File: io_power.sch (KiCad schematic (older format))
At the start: 15 parts

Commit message: Done adding the kitchen sink
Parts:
- added U?: TCA6424A, symbol antboard:TCA6424A
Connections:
- net GND: now also U?.25 (GND), U?.26 (ADDR)
- net PAV10: now also U?.3 (P02)
- net PAV160: now also U?.7 (P06)
- net PAV20: now also U?.4 (P03)
- net PAV40: now also U?.5 (P04)
- net PAV5: now also U?.2 (P01)
- net PAV80: now also U?.6 (P05)
- net PAVEN: now also U?.1 (P00)
- net PBV10: now also U?.10 (P11), U?.17 (P20)
- net PBV160: now also U?.14 (P15), U?.21 (P24)
- net PBV20: now also U?.11 (P12), U?.18 (P21)
- net PBV40: now also U?.12 (P13), U?.19 (P22)
- net PBV5: now also U?.16 (P17), U?.9 (P10)
- net PBV80: now also U?.13 (P14), U?.20 (P23)
- net PBVEN: now also U?.15 (P16), U?.8 (P07)
- net SCL: now also U?.29 (SCL)
- net SDA: now also U?.30 (SDA)
- new net +3V3: U?.27 (VCCP), U?.28 (~RST), U?.31 (VCCI)
- no-connect marks 3 -> 4
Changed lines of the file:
@@
 EESchema Schematic File Version 4
-LIBS:antboard-cache
 EELAYER 30 0
 EELAYER END
@@
 encoding utf-8
 Sheet 5 5
-Title ""
-Date ""
+Title "I/O power supplies"
+Date "2019-11-29"
 Rev ""
 Comp ""
@@
 SCL
 Wire Wire Line
-	1100 1200 1600 1200
-Text Label 1600 1200 2    50   ~ 0
-PAVEN
-Text HLabel 1100 1200 0    50   Input ~ 0
-PAVEN
-Wire Wire Line
-	1100 1300 1600 1300
-Text Label 1600 1300 2    50   ~ 0
-PBVEN
-Text HLabel 1100 1300 0    50   Input ~ 0
-PBVEN
-Wire Wire Line
-	1100 1400 1600 1400
-Text Label 1600 1400 2    50   ~ 0
-PCVEN
-Text HLabel 1100 1400 0    50   Input ~ 0
-PCVEN
-Wire Wire Line
 	7350 5800 7350 5900
 $Comp
@@
 Text Label 6550 5500 0    50   ~ 0
 PBV160
-Wire Wire Line
-	7550 5500 6550 5500
 Text Label 6550 5400 0    50   ~ 0
 PBV80
-Wire Wire Line
-	7550 5400 6550 5400
 Text Label 6550 5300 0    50   ~ 0
 PBV40
-Wire Wire Line
-	7550 5300 6550 5300
 Text Label 6550 5200 0    50   ~ 0
 PBV20
-Wire Wire Line
-	7550 5200 6550 5200
 Text Label 6550 5100 0    50   ~ 0
 PBV10
-Wire Wire Line
-	7550 5100 6550 5100
 Text Label 6550 5000 0    50   ~ 0
 PBV5
-Wire Wire Line
-	7550 5000 6550 5000
 Text Label 6550 3050 0    50   ~ 0
 PBVEN
@@
 Text Label 6550 3750 0    50   ~ 0
 PBV160
-Wire Wire Line
-	7550 3750 6550 3750
 Text Label 6550 3650 0    50   ~ 0
 PBV80
-Wire Wire Line
-	7550 3650 6550 3650
 Text Label 6550 3550 0    50   ~ 0
 PBV40
-Wire Wire Line
-	7550 3550 6550 3550
 Text Label 6550 3450 0    50   ~ 0
 PBV20
-Wire Wire Line
-	7550 3450 6550 3450
 Text Label 6550 3350 0    50   ~ 0
 PBV10
-Wire Wire Line
-	7550 3350 6550 3350
 Text Label 6550 3250 0    50   ~ 0
 PBV5
-Wire Wire Line
-	7550 3250 6550 3250
 Text Label 6550 1300 0    50   ~ 0
 PAVEN
@@
 Text Label 6550 2000 0    50   ~ 0
 PAV160
-Wire Wire Line
-	7550 2000 6550 2000
 Text Label 6550 1900 0    50   ~ 0
 PAV80
-Wire Wire Line
-	7550 1900 6550 1900
 Text Label 6550 1800 0    50   ~ 0
 PAV40
-Wire Wire Line
-	7550 1800 6550 1800
 Text Label 6550 1700 0    50   ~ 0
 PAV20
-Wire Wire Line
-	7550 1700 6550 1700
 Text Label 6550 1600 0    50   ~ 0
 PAV10
-Wire Wire Line
-	7550 1600 6550 1600
 Text Label 6550 1500 0    50   ~ 0
 PAV5
-Wire Wire Line
-	7550 1500 6550 1500
 $Comp
 L Device:R_Small R?
@@
 Connection ~ 7000 4800
 Wire Wire Line
-	7000 4800 6550 4800
-Wire Wire Line
 	7000 3850 7000 3050
 Connection ~ 7000 3050
 Wire Wire Line
-	7000 3050 6550 3050
-Wire Wire Line
 	7000 2100 7000 1300
 Connection ~ 7000 1300
-Wire Wire Line
-	7000 1300 6550 1300
 Wire Wire Line
 	7000 2300 7000 2400
@@
 	1    0    0    -1
 $EndComp
+Wire Wire Line
+	4500 2550 5150 2550
+Wire Wire Line
+	4500 2650 5250 2650
+Wire Wire Line
+	5250 2650 5250 1600
+Wire Wire Line
+	5250 1600 7550 1600
+Wire Wire Line
+	4500 2750 5350 2750
+Wire Wire Line
+	5350 2750 5350 1700
+Wire Wire Line
+	5350 1700 7550 1700
+Wire Wire Line
+	4500 2850 5450 2850
+Wire Wire Line
+	5450 2850 5450 1800
+Wire Wire Line
+	5450 1800 7550 1800
+Wire Wire Line
+	5550 1900 5550 2950
+Wire Wire Line
+	5550 2950 4500 2950
+Wire Wire Line
+	5550 1900 7550 1900
+Wire Wire Line
+	4500 3050 5650 3050
+Wire Wire Line
+	5650 3050 5650 2000
+Wire Wire Line
+	5650 2000 7550 2000
+Wire Wire Line
+	4500 3250 7550 3250
+Wire Wire Line
+	4500 3350 7550 3350
+Wire Wire Line
+	4500 3450 7550 3450
+Wire Wire Line
+	4500 3550 7550 3550
+Wire Wire Line
+	4500 3650 7550 3650
+Wire Wire Line
+	4500 3750 7550 3750
+Wire Wire Line
+	5150 1500 7550 1500
+Wire Wire Line
+	5150 2550 5150 1500
+Wire Wire Line
+	4500 3950 5650 3950
+Wire Wire Line
+	5650 3950 5650 5000
+Wire Wire Line
+	5650 5000 7550 5000
+Wire Wire Line
+	5550 5100 5550 4050
+Wire Wire Line
+	5550 4050 4500 4050
+Wire Wire Line
+	5550 5100 7550 5100
+Wire Wire Line
+	4500 4150 5450 4150
+Wire Wire Line
+	5450 4150 5450 5200
+Wire Wire Line
+	5450 5200 7550 5200
+Wire Wire Line
+	5350 5300 5350 4250
+Wire Wire Line
+	5350 4250 4500 4250
+Wire Wire Line
+	5350 5300 7550 5300
+Wire Wire Line
+	4500 4350 5250 4350
+Wire Wire Line
+	5250 4350 5250 5400
+Wire Wire Line
+	5250 5400 7550 5400
+Wire Wire Line
+	5150 5500 5150 4450
+Wire Wire Line
+	5150 4450 4500 4450
+Wire Wire Line
+	5150 5500 7550 5500
+Wire Wire Line
+	3550 3350 3050 3350
+Wire Wire Line
+	3550 3450 3050 3450
+Text Label 3050 3350 0    50   ~ 0
+SDA
+Text Label 3050 3450 0    50   ~ 0
+SCL
+NoConn ~ 3550 3150
+$Comp
+L power:+3V3 #PWR?
+U 1 1 5DE774F4
+P 4050 2150
+F 0 "#PWR?" H 4050 2000 50  0001 C CNN
+F 1 "+3V3" H 4065 2323 50  0000 C CNN
+F 2 "" H 4050 2150 50  0001 C CNN
+F 3 "" H 4050 2150 50  0001 C CNN
+	1    4050 2150
+	1    0    0    -1
+$EndComp
+Wire Wire Line
+	4000 2250 4000 2200
+Wire Wire Line
+	4000 2200 4050 2200
+Wire Wire Line
+	4100 2200 4100 2250
+Wire Wire Line
+	4050 2150 4050 2200
+Connection ~ 4050 2200
+Wire Wire Line
+	4050 2200 4100 2200
+$Comp
+L power:GND #PWR?
+U 1 1 5DE8B0E0
+P 4050 4950
+AR Path="/5DE8B0E0" Ref="#PWR?"  Part="1"
+AR Path="/5DF7E971/5DE8B0E0" Ref="#PWR?"  Part="1"
+AR Path="/5DFC2583/5DE8B0E0" Ref="#PWR?"  Part="1"
+AR Path="/5EA8F1AB/5DE8B0E0" Ref="#PWR?"  Part="1"
+F 0 "#PWR?" H 4050 4700 50  0001 C CNN
+F 1 "GND" H 4055 4777 50  0000 C CNN
+F 2 "" H 4050 4950 50  0001 C CNN
+F 3 "" H 4050 4950 50  0001 C CNN
+	1    4050 4950
+	1    0    0    -1
+$EndComp
+Wire Wire Line
+	4050 4850 4050 4950
+Wire Wire Line
+	3550 3650 3450 3650
+Wire Wire Line
+	3450 3650 3450 2150
+Wire Wire Line
+	3550 3850 3450 3850
+$Comp
+L power:GND #PWR?
+U 1 1 5DE9ACDD
+P 3450 4950
+AR Path="/5DE9ACDD" Ref="#PWR?"  Part="1"
+AR Path="/5DF7E971/5DE9ACDD" Ref="#PWR?"  Part="1"
+AR Path="/5DFC2583/5DE9ACDD" Ref="#PWR?"  Part="1"
+AR Path="/5EA8F1AB/5DE9ACDD" Ref="#PWR?"  Part="1"
+F 0 "#PWR?" H 3450 4700 50  0001 C CNN
+F 1 "GND" H 3455 4777 50  0000 C CNN
+F 2 "" H 3450 4950 50  0001 C CNN
+F 3 "" H 3450 4950 50  0001 C CNN
+	1    3450 4950
+	1    0    0    -1
+$EndComp
+$Comp
+L power:+3V3 #PWR?
+U 1 1 5DE9B187
+P 3450 2150
+F 0 "#PWR?" H 3450 2000 50  0001 C CNN
+F 1 "+3V3" H 3465 2323 50  0000 C CNN
+F 2 "" H 3450 2150 50  0001 C CNN
+F 3 "" H 3450 2150 50  0001 C CNN
+	1    3450 2150
+	1    0    0    -1
+$EndComp
+Wire Wire Line
+	3450 3850 3450 4950
+$Comp
+L antboard:TCA6424A U?
+U 1 1 5DE0851E
+P 3650 2350
+F 0 "U?" H 3700 2400 50  0000 C CNN
+F 1 "TCA6424A" H 4350 2400 50  0000 C CNN
+F 2 "" H 3650 2350 50  0001 C CNN
+F 3 "" H 3650 2350 50  0001 C CNN
+	1    3650 2350
+	1    0    0    -1
+$EndComp
+Wire Wire Line
+	5050 2450 5050 1300
+Wire Wire Line
+	5050 1300 7000 1300
+Wire Wire Line
+	4500 2450 5050 2450
+Wire Wire Line
+	6450 3150 6450 3050
+Wire Wire Line
+	6450 3050 7000 3050
+Wire Wire Line
+	4500 3150 6450 3150
+Wire Wire Line
+	5750 3850 5750 4800
+Wire Wire Line
+	5750 4800 7000 4800
+Wire Wire Line
+	4500 3850 5750 3850
 $EndSCHEMATC

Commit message: Annotate schematic
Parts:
- U5: renamed from U?; footprint (none) -> Package_DFN_QFN:QFN-32-1EP_5x5mm_P0.5mm_EP3.1x3.1mm
- gave numbers to parts that had none: 15

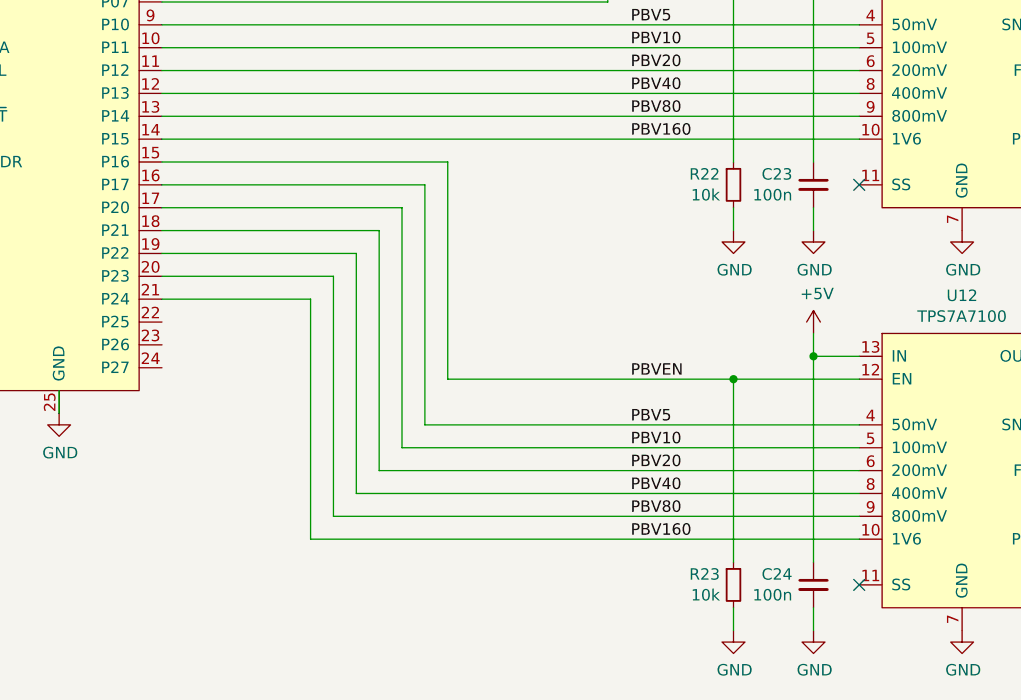
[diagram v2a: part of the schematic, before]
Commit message: Schematic mostly done, place begun
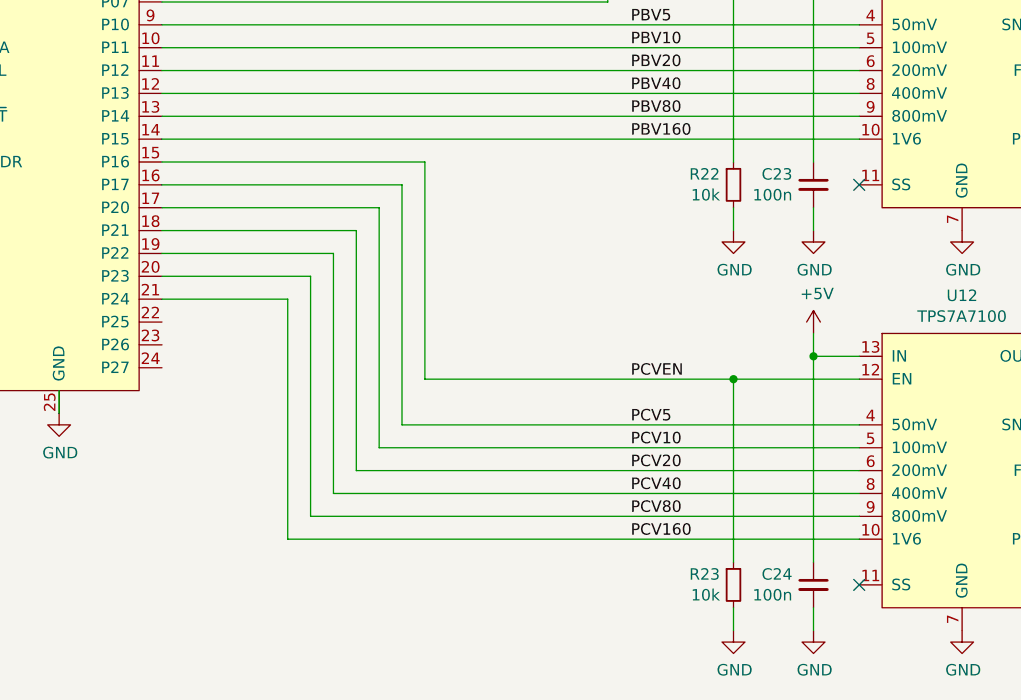
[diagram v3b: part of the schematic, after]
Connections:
- net PBV10: no longer U12.5 (100mV), U5.17 (P20)
- net PBV160: no longer U12.10 (1V6), U5.21 (P24)
- net PBV20: no longer U12.6 (200mV), U5.18 (P21)
- net PBV40: no longer U12.8 (400mV), U5.19 (P22)
- net PBV5: no longer U12.4 (50mV), U5.16 (P17)
- net PBV80: no longer U12.9 (800mV), U5.20 (P23)
- net PBVEN: no longer R23.1, U12.12 (EN), U5.15 (P16)
- new net PCV10: U12.5 (100mV), U5.17 (P20)
- new net PCV160: U12.10 (1V6), U5.21 (P24)
- new net PCV20: U12.6 (200mV), U5.18 (P21)
- new net PCV40: U12.8 (400mV), U5.19 (P22)
- new net PCV5: U12.4 (50mV), U5.16 (P17)
- new net PCV80: U12.9 (800mV), U5.20 (P23)
- new net PCVEN: R23.1, U12.12 (EN), U5.15 (P16)
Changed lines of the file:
@@
 $EndComp
 Text Label 6550 4800 0    50   ~ 0
-PBVEN
+PCVEN
 Wire Wire Line
 	7550 4800 7000 4800
 Text Label 6550 5500 0    50   ~ 0
-PBV160
+PCV160
 Text Label 6550 5400 0    50   ~ 0
-PBV80
+PCV80
 Text Label 6550 5300 0    50   ~ 0
-PBV40
+PCV40
 Text Label 6550 5200 0    50   ~ 0
-PBV20
+PCV20
 Text Label 6550 5100 0    50   ~ 0
-PBV10
+PCV10
 Text Label 6550 5000 0    50   ~ 0
-PBV5
+PCV5
 Text Label 6550 3050 0    50   ~ 0
 PBVEN
@@
 	5150 2550 5150 1500
 Wire Wire Line
-	4500 3950 5650 3950
-Wire Wire Line
-	5650 3950 5650 5000
-Wire Wire Line
-	5650 5000 7550 5000
-Wire Wire Line
-	5550 5100 5550 4050
-Wire Wire Line
-	5550 4050 4500 4050
-Wire Wire Line
-	5550 5100 7550 5100
-Wire Wire Line
-	4500 4150 5450 4150
-Wire Wire Line
-	5450 4150 5450 5200
-Wire Wire Line
-	5450 5200 7550 5200
-Wire Wire Line
-	5350 5300 5350 4250
-Wire Wire Line
-	5350 4250 4500 4250
-Wire Wire Line
-	5350 5300 7550 5300
-Wire Wire Line
-	4500 4350 5250 4350
-Wire Wire Line
-	5250 4350 5250 5400
-Wire Wire Line
-	5250 5400 7550 5400
-Wire Wire Line
-	5150 5500 5150 4450
-Wire Wire Line
-	5150 4450 4500 4450
-Wire Wire Line
-	5150 5500 7550 5500
+	4500 3950 5550 3950
+Wire Wire Line
+	5550 3950 5550 5000
+Wire Wire Line
+	5550 5000 7550 5000
+Wire Wire Line
+	5450 5100 5450 4050
+Wire Wire Line
+	5450 4050 4500 4050
+Wire Wire Line
+	5450 5100 7550 5100
+Wire Wire Line
+	4500 4150 5350 4150
+Wire Wire Line
+	5350 4150 5350 5200
+Wire Wire Line
+	5350 5200 7550 5200
+Wire Wire Line
+	5250 5300 5250 4250
+Wire Wire Line
+	5250 4250 4500 4250
+Wire Wire Line
+	5250 5300 7550 5300
+Wire Wire Line
+	4500 4350 5150 4350
+Wire Wire Line
+	5150 4350 5150 5400
+Wire Wire Line
+	5150 5400 7550 5400
+Wire Wire Line
+	5050 5500 5050 4450
+Wire Wire Line
+	5050 4450 4500 4450
+Wire Wire Line
+	5050 5500 7550 5500
 Wire Wire Line
 	3550 3350 3050 3350
@@
 	4500 3150 6450 3150
 Wire Wire Line
-	5750 3850 5750 4800
-Wire Wire Line
-	5750 4800 7000 4800
-Wire Wire Line
-	4500 3850 5750 3850
+	5650 3850 5650 4800
+Wire Wire Line
+	5650 4800 7000 4800
+Wire Wire Line
+	4500 3850 5650 3850
 $EndSCHEMATC

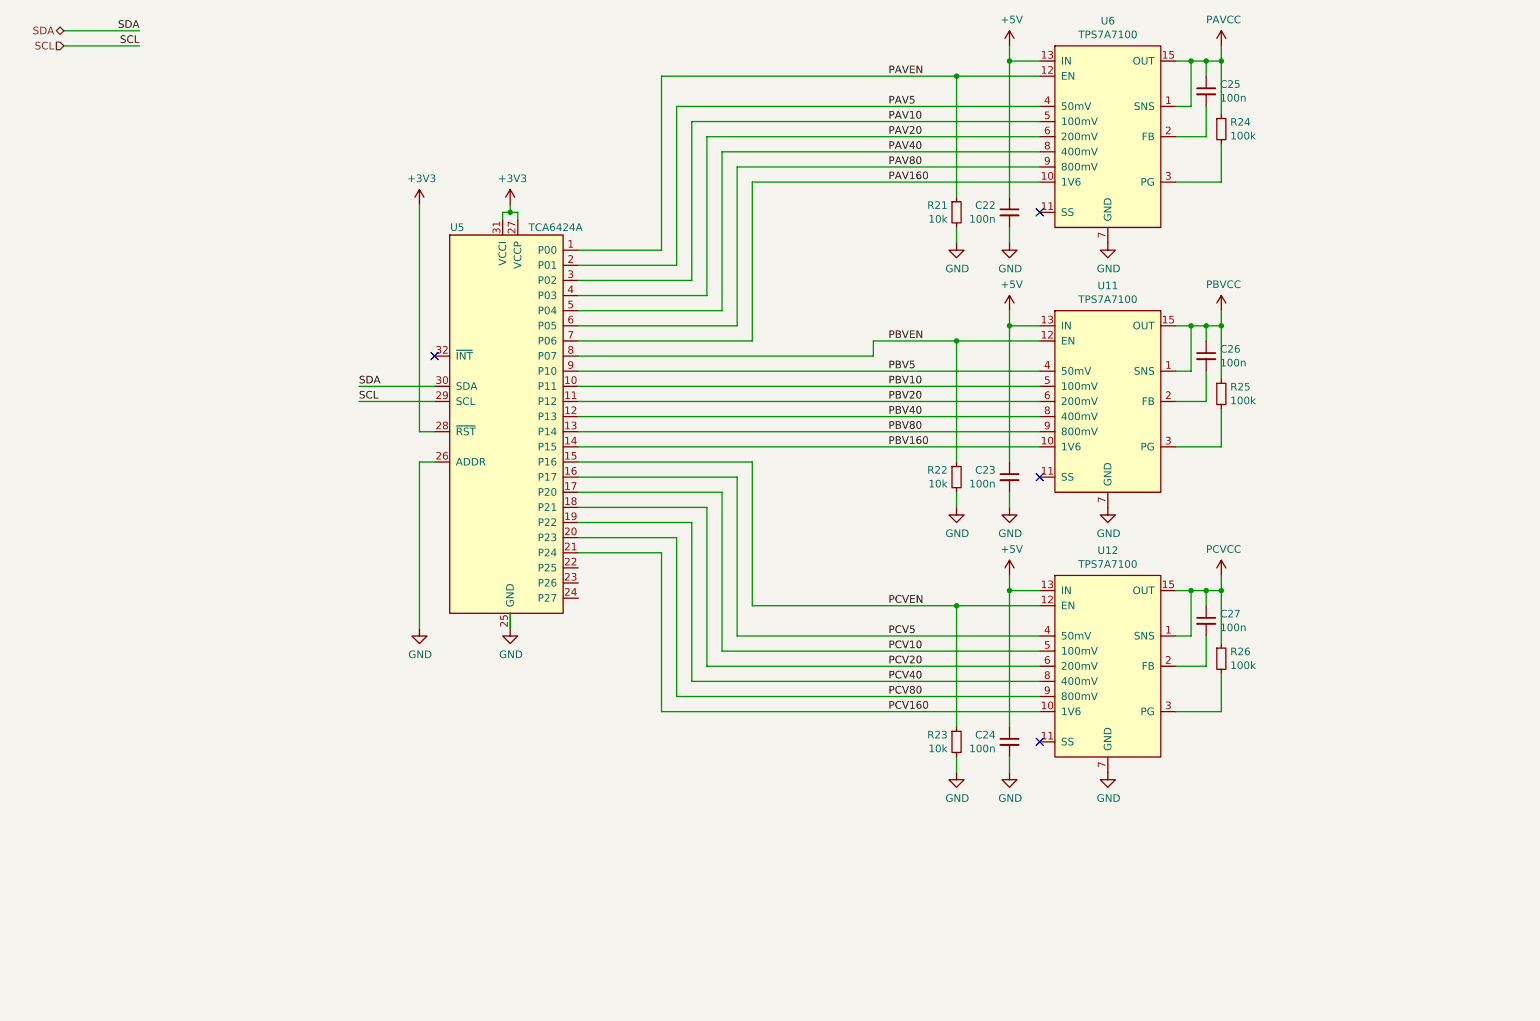
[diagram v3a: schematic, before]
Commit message: Misc sch fixes and psu p&r done
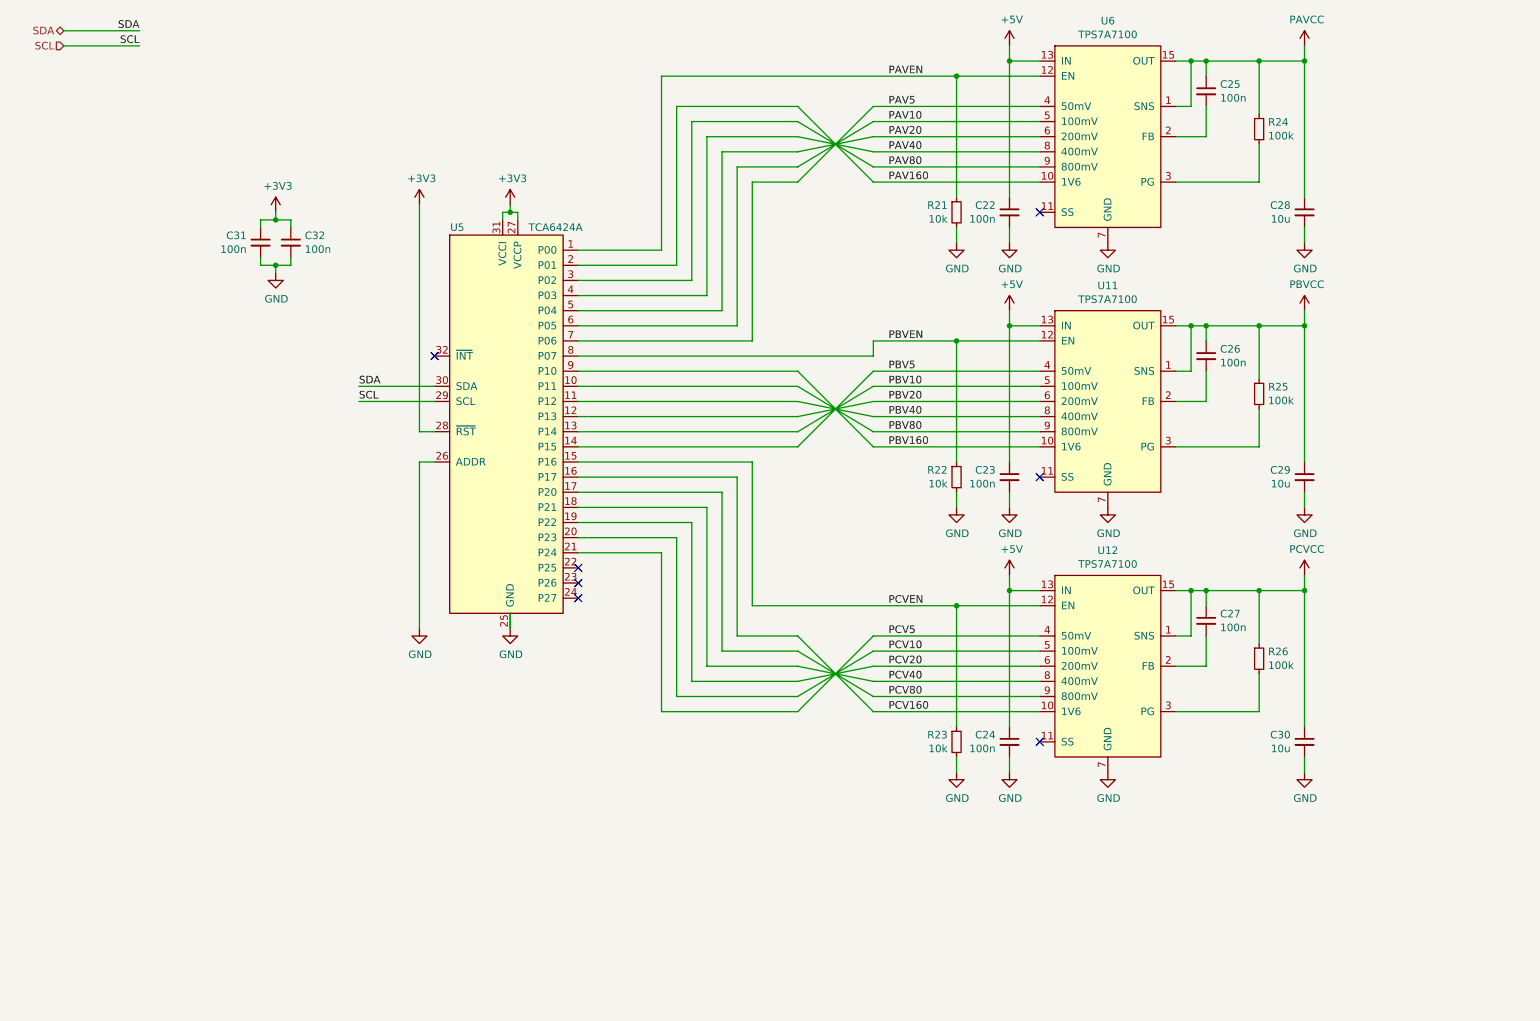
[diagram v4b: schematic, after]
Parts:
- added C28, C29, C30: 10u, Capacitor_SMD:C_0603_1608Metric, symbol Device:C_Small
- added C31, C32: 100n, Capacitor_SMD:C_0603_1608Metric, symbol Device:C_Small
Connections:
- net +3V3: now also C31.1, C32.1
- net GND: now also C28.2, C29.2, C30.2, C31.2, C32.2
- net PAV10: now also U5.6 (P05); no longer U5.3 (P02)
- net PAV160: now also U5.2 (P01); no longer U5.7 (P06)
- net PAV20: now also U5.5 (P04); no longer U5.4 (P03)
- net PAV40: now also U5.4 (P03); no longer U5.5 (P04)
- net PAV5: now also U5.7 (P06); no longer U5.2 (P01)
- net PAV80: now also U5.3 (P02); no longer U5.6 (P05)
- net PAVCC: now also C28.1
- net PBV10: now also U5.13 (P14); no longer U5.10 (P11)
- net PBV160: now also U5.9 (P10); no longer U5.14 (P15)
- net PBV20: now also U5.12 (P13); no longer U5.11 (P12)
- net PBV40: now also U5.11 (P12); no longer U5.12 (P13)
- net PBV5: now also U5.14 (P15); no longer U5.9 (P10)
- net PBV80: now also U5.10 (P11); no longer U5.13 (P14)
- net PBVCC: now also C29.1
- net PCV10: now also U5.20 (P23); no longer U5.17 (P20)
- net PCV160: now also U5.16 (P17); no longer U5.21 (P24)
- net PCV20: now also U5.19 (P22); no longer U5.18 (P21)
- net PCV40: now also U5.18 (P21); no longer U5.19 (P22)
- net PCV5: now also U5.21 (P24); no longer U5.16 (P17)
- net PCV80: now also U5.17 (P20); no longer U5.20 (P23)
- net PCVCC: now also C30.1
- no-connect marks 4 -> 7
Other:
- moved on the sheet: R24, R25, R26
